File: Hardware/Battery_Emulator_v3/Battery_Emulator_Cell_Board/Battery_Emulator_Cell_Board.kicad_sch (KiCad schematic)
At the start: 46 parts, among them J3 Cell1_Vout, J4 Conn_01x05, Q1 IRFB7545PBF, Q2 MJE2955T, Q3 MJE2955T, U1 LT3080xQ, U2 ISO1640BDR, U3 MCP4651T-103E_ST, U4 KA78M05_TO252, U5 MCP6001UT-I/OT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

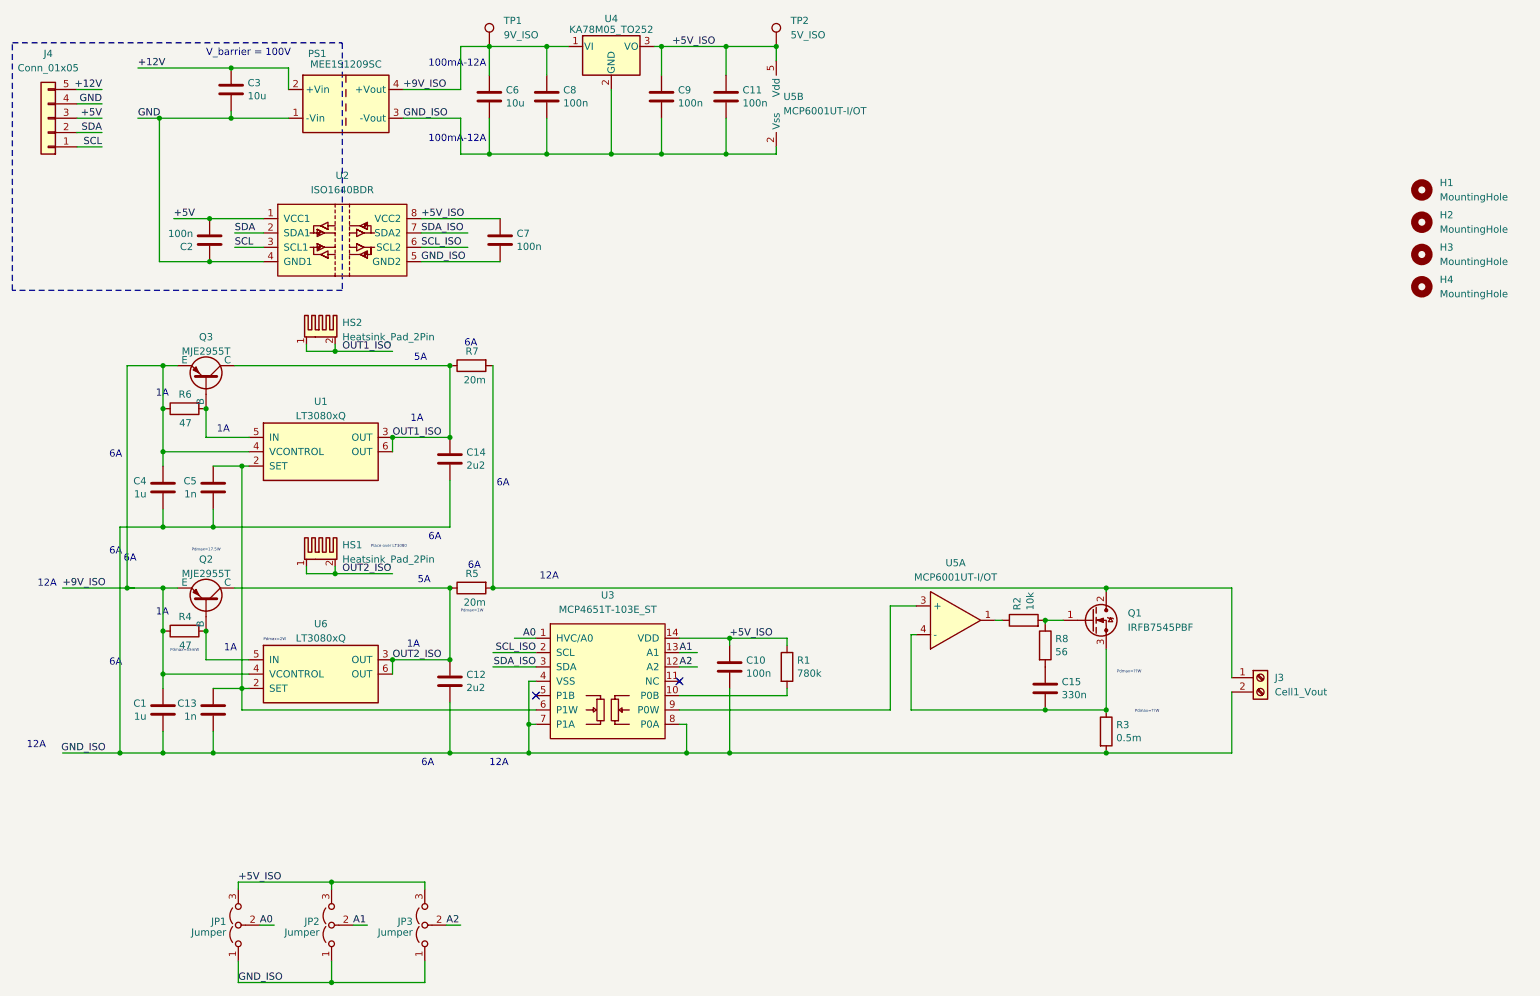
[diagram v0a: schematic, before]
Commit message: Update Cell board
Finished PCB layout design.
Added two capacitors in schematic for stable feedback network for current sink.
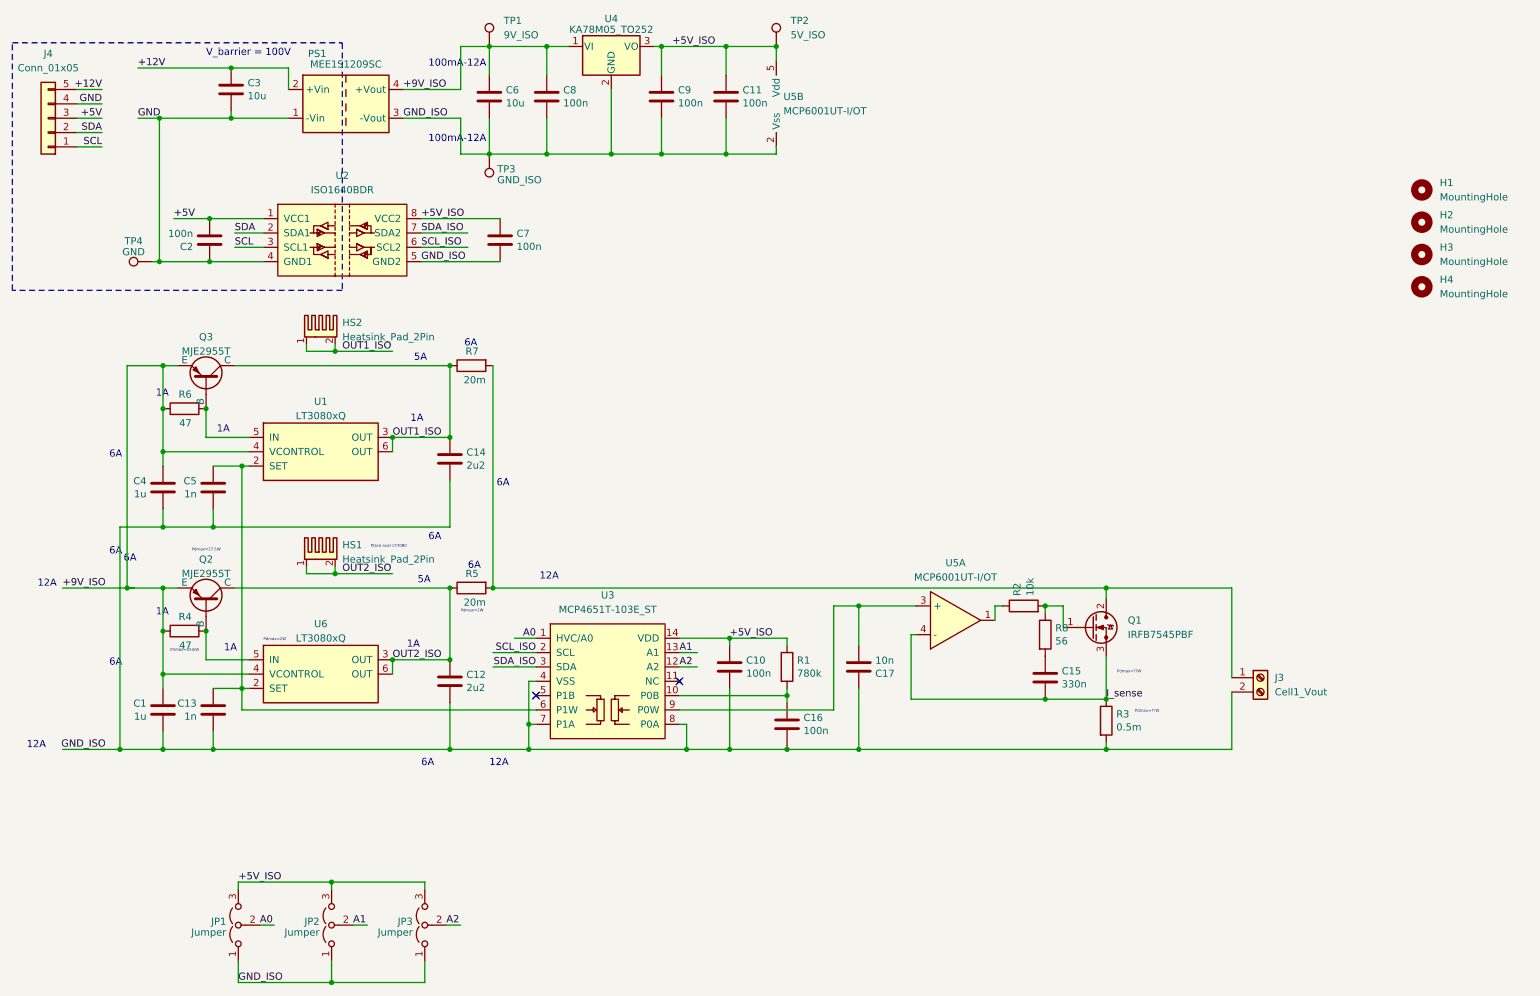
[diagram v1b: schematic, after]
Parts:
- added C16: 100n, Capacitor_SMD:C_0805_2012Metric, symbol Device:C
- added C17: 10n, Capacitor_SMD:C_0805_2012Metric, symbol Device:C
- added TP3: GND_ISO, TestPoint:TestPoint_Pad_D2.5mm, symbol Connector:TestPoint
- added TP4: GND, TestPoint:TestPoint_Pad_D2.5mm, symbol Connector:TestPoint
- H1, H2, H3, H4: footprint MountingHole:MountingHole_3.2mm_M3 -> MountingHole:MountingHole_3.2mm_M3_DIN965_Pad
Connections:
- net GND: now also TP4.1
- net GND_ISO: now also C16.2, C17.1, TP3.1
- net I_sense: now reaches C15.2, Q1.3, R3.1, U5.4 (-)
- net at R1.2, U3.10 (P0B): now also C16.1
- net at U3.9 (P0W), U5.3 (+): now also C17.2
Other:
- moved on the sheet: C15, Q1, R2, R3, R8
